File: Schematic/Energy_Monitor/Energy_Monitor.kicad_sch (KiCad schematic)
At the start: 9 parts, among them J1 I2C LCD, J2 SD Card Module, J3 RTC, J4 PZEM-004T, U1 L7805, U2 LM2596, U3 Level_Shifter, U4 ESP32-WROOM-32

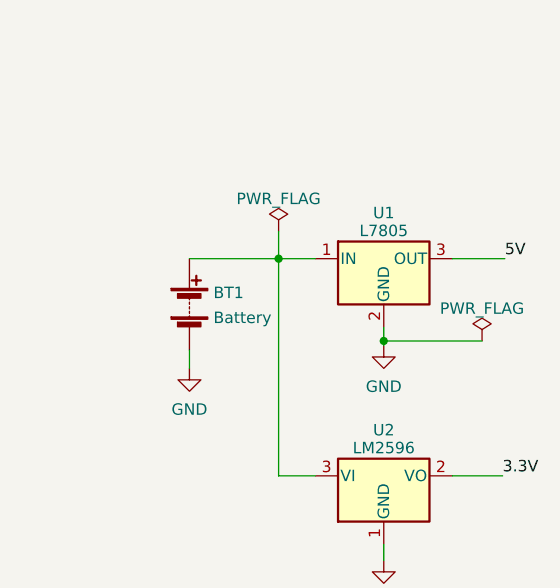
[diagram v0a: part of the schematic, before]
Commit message: Update
- Added a switch to the design
- Changed SD card logging interval to 20s
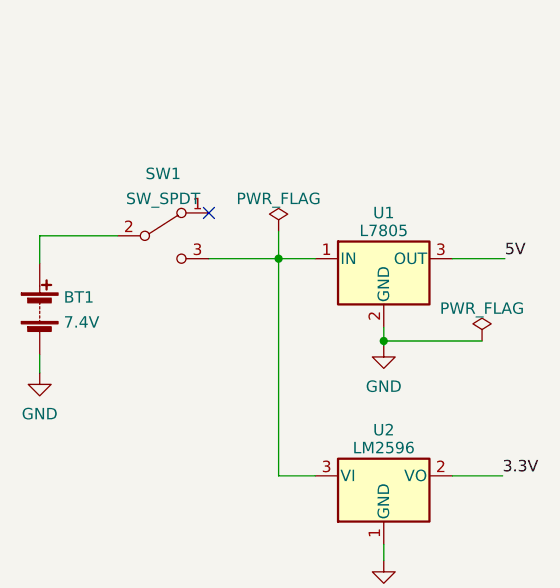
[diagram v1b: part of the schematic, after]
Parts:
- added SW1: SW_SPDT, symbol Switch:SW_SPDT
- BT1: value Battery -> 7.4V
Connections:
- net at U1.1 (IN), U2.3 (VI): now also SW1.3 (C); no longer BT1.1 (+)
- new net: BT1.1 (+), SW1.2 (B)
- no-connect marks 25 -> 26
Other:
- moved on the sheet: BT1
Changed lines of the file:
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@@
   (no_connect (at 167.132 131.064))
   (no_connect (at 167.132 128.524))
+  (no_connect (at 95.123 74.676))
   (no_connect (at 167.132 90.424))
   (no_connect (at 167.132 95.504))
@@
     (stroke (width 0) (type default) (color 0 0 0 0))
   )
+  (wire (pts (xy 76.327 80.264) (xy 76.327 77.216))
+    (stroke (width 0) (type default) (color 0 0 0 0))
+  )
+  (wire (pts (xy 76.327 77.216) (xy 84.963 77.216))
+    (stroke (width 0) (type default) (color 0 0 0 0))
+  )
   (wire (pts (xy 151.892 146.304) (xy 151.892 148.336))
     (stroke (width 0) (type default) (color 0 0 0 0))
   )
-  (wire (pts (xy 92.964 89.916) (xy 92.964 91.948))
+  (wire (pts (xy 76.327 90.424) (xy 76.327 92.456))
+    (stroke (width 0) (type default) (color 0 0 0 0))
+  )
+  (wire (pts (xy 95.123 79.756) (xy 102.87 79.756))
     (stroke (width 0) (type default) (color 0 0 0 0))
   )
@@
   )
   (wire (pts (xy 186.944 134.112) (xy 193.548 134.112))
-    (stroke (width 0) (type default) (color 0 0 0 0))
-  )
-  (wire (pts (xy 92.964 79.756) (xy 102.87 79.756))
     (stroke (width 0) (type default) (color 0 0 0 0))
   )
@@
     (pin "1")
   )
-  (symbol (lib_id "power:GND") (at 92.964 91.948 0) (unit 1)
-    (in_bom yes) (on_board yes) (fields_autoplaced)
-    (property "Reference" "#PWR01" (id 0) (at 92.964 98.298 0)
-      (effects (font (size 1.27 1.27)) hide)
-    )
-    (property "Value" "GND" (id 1) (at 92.964 96.5105 0))
-    (property "Footprint" "" (id 2) (at 92.964 91.948 0)
-      (effects (font (size 1.27 1.27)) hide)
-    )
-    (property "Datasheet" "" (id 3) (at 92.964 91.948 0)
+  (symbol (lib_id "power:GND") (at 76.327 92.456 0) (unit 1)
+    (in_bom yes) (on_board yes) (fields_autoplaced)
+    (property "Reference" "#PWR01" (id 0) (at 76.327 98.806 0)
+      (effects (font (size 1.27 1.27)) hide)
+    )
+    (property "Value" "GND" (id 1) (at 76.327 97.0185 0))
+    (property "Footprint" "" (id 2) (at 76.327 92.456 0)
+      (effects (font (size 1.27 1.27)) hide)
+    )
+    (property "Datasheet" "" (id 3) (at 76.327 92.456 0)
       (effects (font (size 1.27 1.27)) hide)
     )
@@
     (pin "1")
   )
-  (symbol (lib_id "Device:Battery") (at 92.964 84.836 0) (unit 1)
-    (in_bom yes) (on_board yes) (fields_autoplaced)
-    (property "Reference" "BT1" (id 0) (at 95.631 83.5465 0)
+  (symbol (lib_id "Device:Battery") (at 76.327 85.344 0) (unit 1)
+    (in_bom yes) (on_board yes) (fields_autoplaced)
+    (property "Reference" "BT1" (id 0) (at 78.994 84.0545 0)
       (effects (font (size 1.27 1.27)) (justify left))
     )
-    (property "Value" "Battery" (id 1) (at 95.631 86.3216 0)
+    (property "Value" "7.4V" (id 1) (at 78.994 86.8296 0)
       (effects (font (size 1.27 1.27)) (justify left))
     )
-    (property "Footprint" "" (id 2) (at 92.964 83.312 90)
-      (effects (font (size 1.27 1.27)) hide)
-    )
-    (property "Datasheet" "~" (id 3) (at 92.964 83.312 90)
+    (property "Footprint" "" (id 2) (at 76.327 83.82 90)
+      (effects (font (size 1.27 1.27)) hide)
+    )
+    (property "Datasheet" "~" (id 3) (at 76.327 83.82 90)
       (effects (font (size 1.27 1.27)) hide)
     )
@@
     (pin "1")
   )
+  (symbol (lib_id "Switch:SW_SPDT") (at 90.043 77.216 0) (unit 1)
+    (in_bom yes) (on_board yes) (fields_autoplaced)
+    (property "Reference" "SW1" (id 0) (at 90.043 70.3285 0))
+    (property "Value" "SW_SPDT" (id 1) (at 90.043 73.1036 0))
+    (property "Footprint" "" (id 2) (at 90.043 77.216 0)
+      (effects (font (size 1.27 1.27)) hide)
+    )
+    (property "Datasheet" "~" (id 3) (at 90.043 77.216 0)
+      (effects (font (size 1.27 1.27)) hide)
+    )
+    (pin "1")
+    (pin "2")
+    (pin "3")
+  )
   (symbol (lib_id "Connector:Conn_01x06_Male") (at 181.864 131.572 0) (unit 1)
     (in_bom yes) (on_board yes)
@@
     )
     (path "/666713b0-70f4-42df-8761-f65bc212d03b"
-      (reference "BT1") (unit 1) (value "Battery") (footprint "")
+      (reference "BT1") (unit 1) (value "7.4V") (footprint "")
     )
     (path "/299e4937-4c28-477f-ad0b-a3034df93b47"
@@
       (reference "J4") (unit 1) (value "PZEM-004T") (footprint "")
     )
+    (path "/da8c55c6-63df-473c-9e1e-fdce7c38b264"
+      (reference "SW1") (unit 1) (value "SW_SPDT") (footprint "")
+    )
     (path "/2629f374-664b-4a6a-877f-847eba3a2928"

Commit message: Add files via upload
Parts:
- removed J1: I2C LCD, symbol Connector:Conn_01x04_Male
- removed J2: SD Card Module, symbol Connector:Conn_01x06_Male
- removed J3: RTC, symbol Connector:Conn_01x04_Male
- added J1: Micro_SD_Card, symbol Connector:Micro_SD_Card
- added J5: AC-DC Adapter, symbol Connector:Jack-DC
- added RV1: R_Potentiometer, symbol Device:R_Potentiometer
- added U5: LCD, Display:EA_T123X-I2C, symbol Display_Character:EA_T123X-I2C
- added U6: DS3231M, Package_SO:SOIC-16W_7.5x10.3mm_P1.27mm, symbol Timer_RTC:DS3231M
- BT1: value 7.4V -> 3V
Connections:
- net 3.3V: now also J1.2 (VDD)
- net 5V: now also RV1.1, U5.2 (VDD), U5.3 (VLCD), U6.2 (VCC)
- net CS: now also J1.1 (CS)
- net GND: now also J1.4 (VSS), J5.2, RV1.3, U5.1 (VSS), U6.10 (GND), U6.11 (GND), U6.12 (GND), U6.13 (GND), U6.5 (GND), U6.6 (GND), U6.7 (GND), U6.8 (GND), U6.9 (GND)
- net MISO: now also J1.5 (MISO)
- net MOSI: now also J1.6 (MOSI)
- net SCK: now also J1.3 (CLK)
- net SCL: now also U5.6 (SCL), U6.16 (SCL)
- net SDA: now also U5.5 (SDA), U6.15 (SDA)
- net at BT1.1 (+): now also U6.14 (VBAT); no longer SW1.2 (B)
- new net: RV1.2, U5.4 (V0)
- new net: J5.1, SW1.2 (B)
- no-connect marks 26 -> 29
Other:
- note added: "9V Output"
- note added: "DS3231M: Real-time Clock"
- note added: "SMART ENERGY MONITORING SYSTEM"
- note removed: "AUTOMATIC DATA LOGGING SYSTEM (ENERGY MONITOR)"
- moved on the sheet: J4, SW1, U1, U2, U3, U4

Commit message: Add files via upload
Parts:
- removed J4: PZEM-004T, symbol Connector:Conn_01x04_Male
- added U7: PZEM-004T Power Module, Package_LGA:Bosch_LGA-8_2.5x2.5mm_P0.65mm_ClockwisePinNumbering, symbol Sensor:BME280
- J1: value Micro_SD_Card -> Micro SD Card Module
- U1: value L7805 -> L7805 Voltage Regulator
- U2: value LM2596 -> LM2596 Buck Converter
- U3: value Level_Shifter -> Level Shifter
- U4: value ESP32-WROOM-32 -> ESP32 SoC
- U5: value LCD -> 16x2 I2C LCD Module
- U6: value DS3231M -> DS3231 Real-Time Clock
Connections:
- net 5V: now also U7.1 (VCC)
- net GND: now also U7.4 (GND)
- net PZEM_RX: now also U7.2 (PZEM_RX)
- net PZEM_TX: now also U7.3 (PZEM_TX)
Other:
- note added: "SoC: System-on-chip"
- note removed: "DS3231M: Real-time Clock"
